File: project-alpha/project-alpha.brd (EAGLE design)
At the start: 68.6 x 53.3 mm, 0 parts

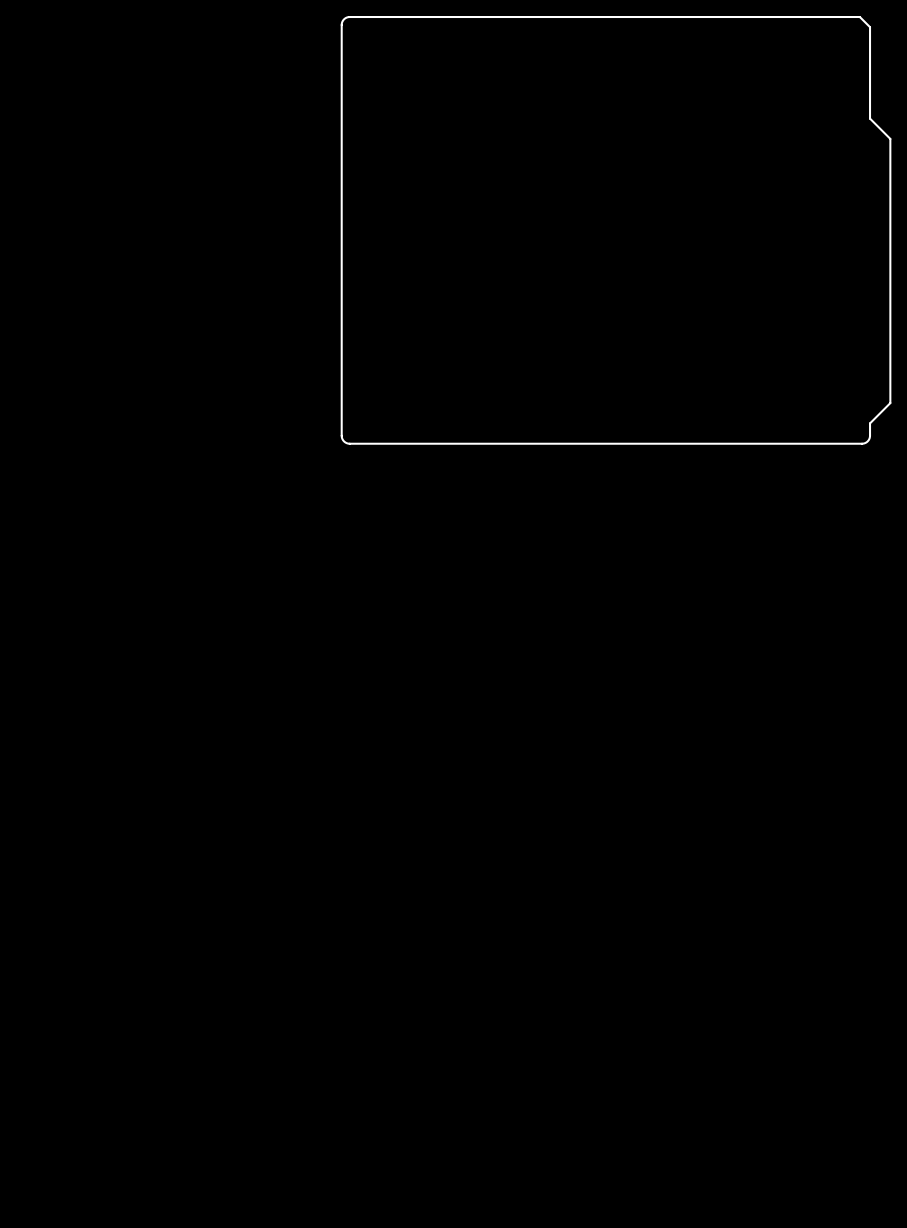
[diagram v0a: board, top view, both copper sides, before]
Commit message: Schematic entry for most parts of project alpha
Design has WiFi module, I2C EEPROM, LDO, LED, SD card, and matching
circuit for antenna.  The antenna isn't included yet as that part
still needs to be created in the library (going with the ACX reference
design part).

Also included solder jumper pads for end user customizations for I2C
EEPROM address, SD card chip select and CC3000 chip select.  These will
be on the back side of the board for easy customization and rewiring.
The user would need to cut the thin trace (10mil) and then resolder to
the pin they want to use (as well as change the software accordingly).

Signed-off-by: fangsuei <fangsuei@fangsuei.com>
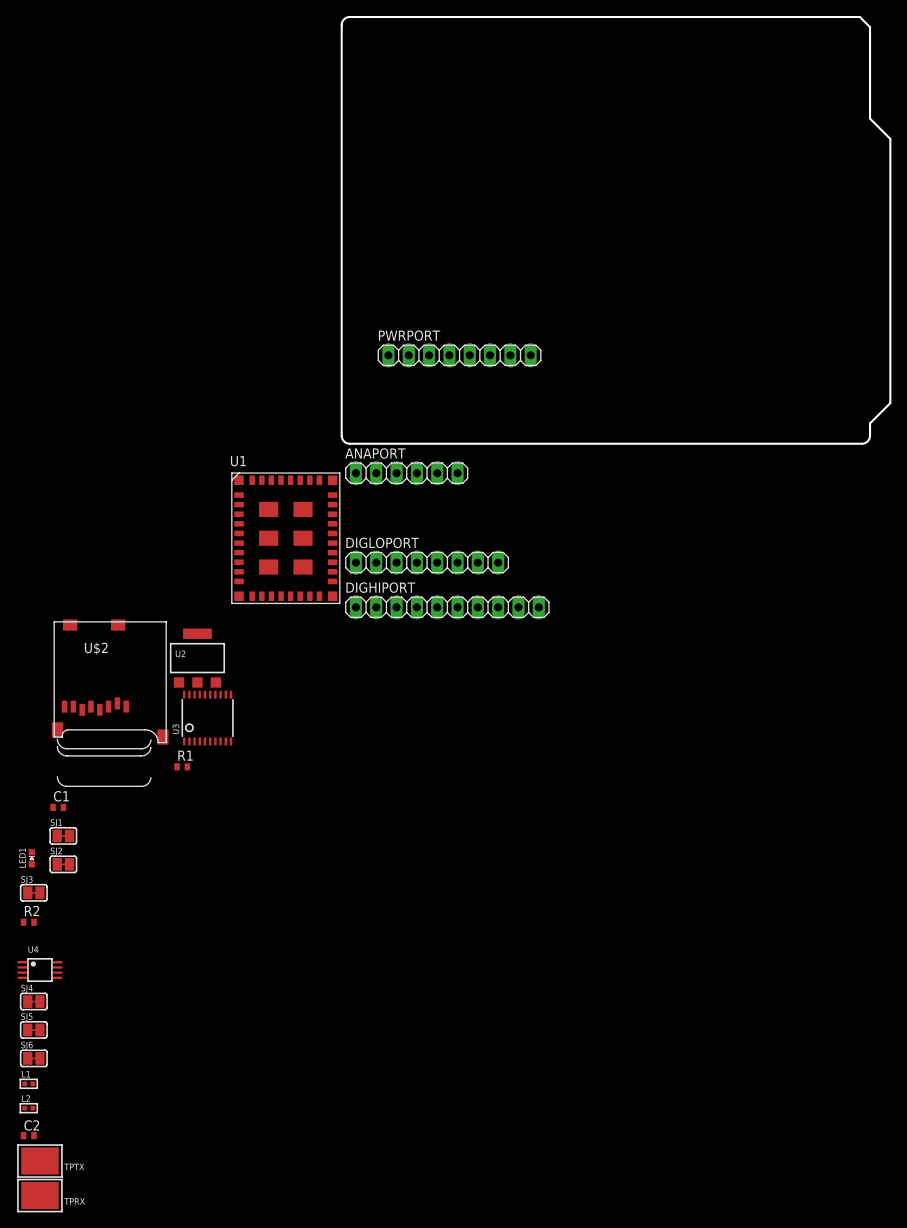
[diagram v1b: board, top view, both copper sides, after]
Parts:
- added ANAPORT: (no value), pinhead:1X06
- added C1: (no value), resistor:C0402
- added C2: (no value), rcl:C0402
- added DIGHIPORT: (no value), pinhead:1X10
- added DIGLOPORT, PWRPORT: (no value), pinhead:1X08
- added L1, L2: (no value), microbuilder:_0402
- added LED1: (no value), microbuilder:CHIPLED_0603_NOOUTLINE
- added R1, R2: 0, resistor:R0402
- added SJ1, SJ2, SJ3, SJ4, SJ5, SJ6: (no value), microbuilder:SOLDERJUMPER_CLOSEDWIRE
- added TPRX, TPTX: (no value), microbuilder:TESTPOINT_SMT
- added U$2: MICROSD, adafruit:MICROSD
- added U1: CC3000-MOD, eightbitlabs:CC3000-LGA
- added U2: TLV1117-33, eightbitlabs:SOT223-R
- added U3: TXS0108E, eightbitlabs:TSSOP20
- added U4: 24AA512, eightbitlabs:TSSOP8
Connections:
- new net +3V3: PWRPORT.4, R1.1, R2.1, U$2.4, U1.23, U2.2, U3.2
- new net +5V: U3.10, U3.19, U4.8
- new net GND: L1.1, L2.1, PWRPORT.6, PWRPORT.7, SJ4.1, SJ5.1, SJ6.1, U$2.6, U$2.MT1, U$2.MT2, U1.1, U1.10, U1.11, U1.16, U1.18, U1.20, U1.22, U1.25, U1.31, U1.32, U1.33, U1.34, U1.36, U1.37, U1.38, U1.39, U1.40, U1.41, U1.42, U1.43, U1.44, U1.45, U1.46, U1.9, U2.1, U2.4, U3.11, U4.4, U4.7
- new net N$1: PWRPORT.5, U2.3
- new net N$10: C1.1, C2.1, L1.2
- new net N$11: DIGHIPORT.6, U3.16
- new net N$12: U1.27, U1.29
- new net N$13: U1.28, U1.30
- new net N$14: DIGHIPORT.7, U3.17
- new net N$15: DIGHIPORT.5, U3.18
- new net N$16: U$2.2, U3.8
- new net N$17: SJ1.1, U3.20
- new net N$18: DIGHIPORT.8, SJ1.2
- new net N$19: SJ2.1, U3.13
- new net N$2: U1.12, U3.1
- new net N$20: DIGLOPORT.4, SJ2.2
- new net N$21: LED1.A, R2.2
- new net N$22: LED1.C, SJ3.1
- new net N$23: DIGLOPORT.5, SJ3.2
- new net N$24: SJ4.2, U4.1
- new net N$25: SJ5.2, U4.2
- new net N$26: SJ6.2, U4.3
- new net N$27: DIGHIPORT.1, U4.6
- new net N$28: DIGHIPORT.2, U4.5
- new net N$29: C2.2, L2.2
- new net N$3: U$2.5, U1.17, U3.3
- new net N$30: TPTX.P$1, U1.6
- new net N$31: TPRX.P$1, U1.8
- new net N$4: U$2.3, U1.15, U3.4
- new net N$5: U$2.7, U1.13, U3.5
- new net N$6: U1.14, U3.6
- new net N$7: U1.26, U3.7
- new net N$8: C1.2, U1.35
- new net N$9: R1.2, U1.19
